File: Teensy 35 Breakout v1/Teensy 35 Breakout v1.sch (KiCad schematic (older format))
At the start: 37 parts, among them P1 CONN_01X13, P10 CONN_01X13, P10a1 CONN_01X10, P11 CONN_01X03, P12 CONN_01X04, P13 CONN_02X04, P14 CONN_02X03, P15 CONN_02X05, P16 CONN_01X03, P17 CONN_01X01, P18 CONN_01X02, P19 CONN_01X08, P1a1 CONN_01X09, P2 CONN_01X13, P20 CONN_01X05, P21 CONN_01X05, P22 CONN_01X04, P23 CONN_01X04, P24 CONN_01X05, P25 CONN_01X10, P26 CONN_01X10, P27 CONN_01X10, P28 CONN_01X10, P2a1 CONN_01X09, P2a2 CONN_01X03, P2a3 CONN_01X03, P3 CONN_01X03, P4 CONN_01X24, P5 CONN_01X24, P6 CONN_01X03, P7 CONN_01X24, P8 CONN_01X24, P9 CONN_01X13, P9a1 CONN_01X09, SW1 SW_PUSH_SMALL_H, SW2 SW_PUSH_SMALL_H

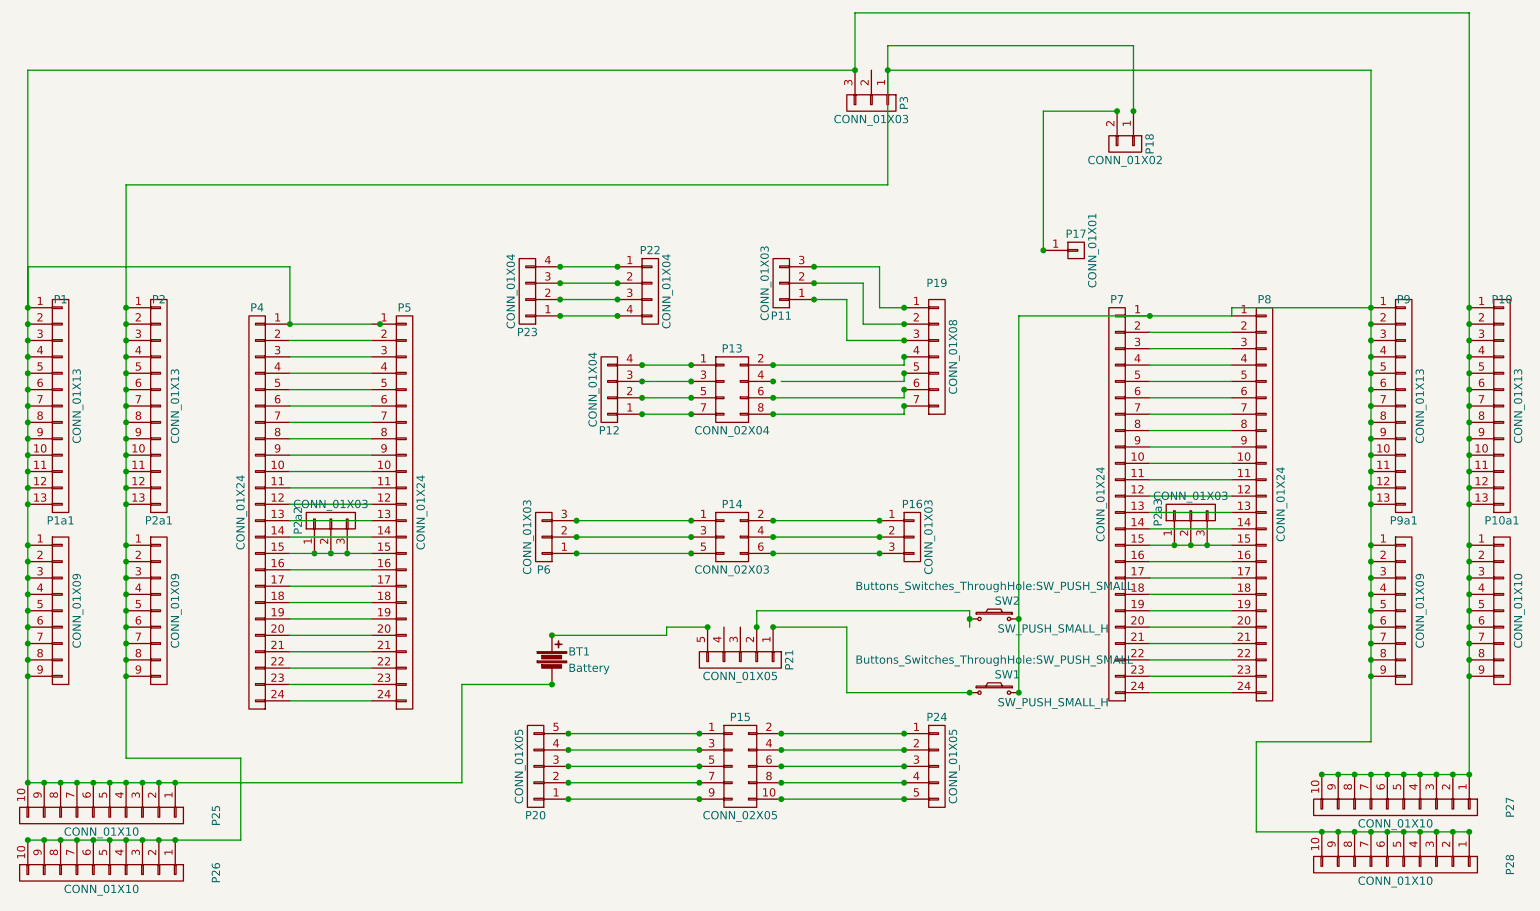
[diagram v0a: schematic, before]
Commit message: corrected reset voltage to 3.3v
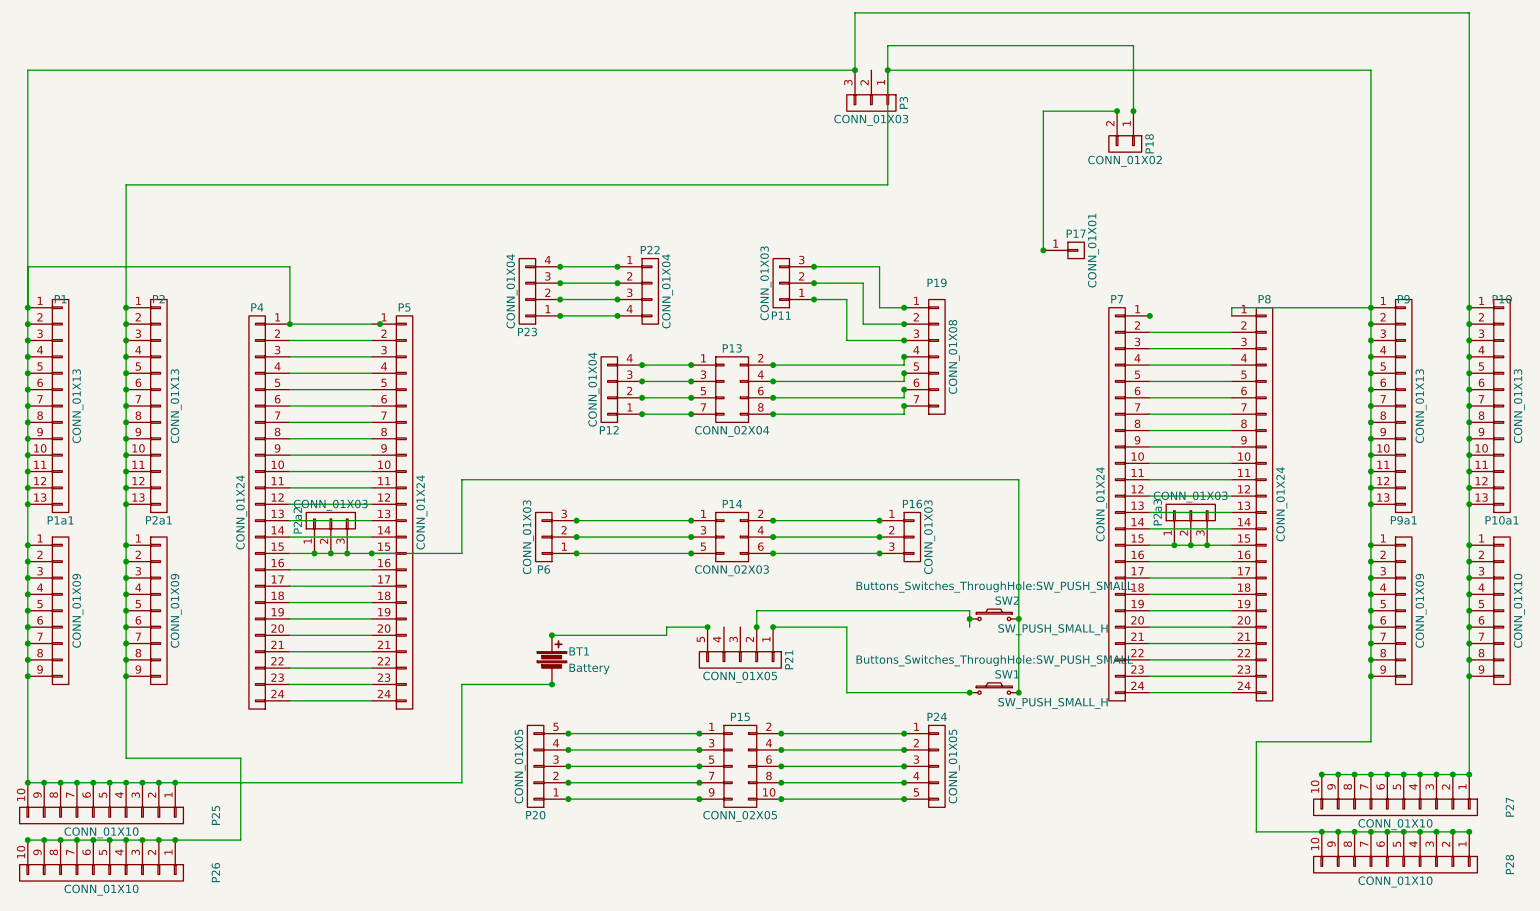
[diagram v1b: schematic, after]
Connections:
- net at P2a2.1 (P1), P2a2.2 (P2), P2a2.3 (P3)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: now also SW1.2, SW2.2
- net at P18.1 (P1), P2.1 (P1), P2.10 (P10)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: no longer P7.1 (P1), SW1.2, SW2.2
- net at P13.4 (P4): now also P19.5 (P5)
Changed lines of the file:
@@
 EESchema Schematic File Version 2
-LIBS:Test-rescue
 LIBS:power
 LIBS:device
@@
 LIBS:contrib
 LIBS:valves
-LIBS:Test-cache
+LIBS:Teensy 35 Breakout v1-cache
 EELAYER 25 0
 EELAYER END
@@
 	8300 2550 7800 2550
 Wire Wire Line
-	7000 2450 8300 2450
-Wire Wire Line
 	3050 4800 2550 4800
 Wire Wire Line
@@
 	2550 4000 3050 4000
 Wire Wire Line
-	2550 3900 3050 3900
+	2550 3900 3600 3900
 Wire Wire Line
 	2550 3800 3050 3800
@@
 	6300 2950 6300 2900
 Wire Wire Line
-	5550 2850 6300 2850
-Wire Wire Line
-	6300 2850 6300 2800
-Wire Wire Line
 	5500 2750 6300 2750
 Wire Wire Line
@@
 Connection ~ 7700 1200
 Connection ~ 7800 2450
-Wire Wire Line
-	7000 2450 7000 4750
 Connection ~ 3100 2500
 Wire Wire Line
@@
 Wire Wire Line
 	950  2150 950  2400
+Wire Wire Line
+	5500 2850 6300 2850
+Wire Wire Line
+	6300 2850 6300 2800
+Wire Wire Line
+	7000 3450 7000 4750
+Wire Wire Line
+	7000 3450 3600 3450
+Wire Wire Line
+	3600 3450 3600 3900
+Connection ~ 3050 3900
 $EndSCHEMATC

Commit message: Additional corrections
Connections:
- net at P2a2.1 (P1), P2a2.2 (P2), P2a2.3 (P3)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: no longer SW1.2, SW2.2
- net at P2a3.1 (P1), P2a3.2 (P2), P2a3.3 (P3)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: now also SW1.2, SW2.2
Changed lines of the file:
@@
 	8300 3950 7800 3950
 Wire Wire Line
-	7800 3850 8300 3850
+	7000 3850 8300 3850
 Wire Wire Line
 	7800 3750 8300 3750
@@
 Wire Wire Line
 	2550 4000 3050 4000
-Wire Wire Line
-	2550 3900 3600 3900
 Wire Wire Line
 	2550 3800 3050 3800
@@
 Wire Wire Line
 	6300 2850 6300 2800
-Wire Wire Line
-	7000 3450 7000 4750
-Wire Wire Line
-	7000 3450 3600 3450
-Wire Wire Line
-	3600 3450 3600 3900
 Connection ~ 3050 3900
+Wire Wire Line
+	3050 3900 2550 3900
+Wire Wire Line
+	7000 4750 7000 3850
+Connection ~ 7800 3850
 $EndSCHEMATC
